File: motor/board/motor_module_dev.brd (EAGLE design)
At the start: 53.3 x 76.2 mm, 97 parts, among them IC6 LTC6088, IC7 DRV8833RTY

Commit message: Board and component orders placed
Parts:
- R2: value 5k -> 5k1
- R42: value 480R -> 470R
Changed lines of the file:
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@@
 <attribute name="VALUE" x="41.5798" y="54.2036" size="1.016" layer="27" font="vector" ratio="20" rot="R180"/>
 </element>
-<element name="R2" library="biomimetic" package="0402-RES" value="5k" x="8.255" y="33.655" smashed="yes" rot="R180">
+<element name="R2" library="biomimetic" package="0402-RES" value="5k1" x="8.255" y="33.655" smashed="yes" rot="R180">
 <attribute name="VALUE" x="7.3295" y="34.363" size="1.016" layer="27" font="vector" ratio="20" rot="R180"/>
 </element>
@@
 <attribute name="VALUE" x="18.488" y="39.6605" size="1.016" layer="27" font="vector" ratio="20" rot="R90"/>
 </element>
-<element name="C42" library="biomimetic" package="0402-CAP" value="2.2nF" x="34.29" y="36.83" smashed="yes" rot="R270"/>
+<element name="C42" library="biomimetic" package="0402-CAP" value="2.2nF" x="34.29" y="36.83" smashed="yes" rot="R270">
+<attribute name="VOLTAGE" value="6.3V" x="34.29" y="36.83" size="1.778" layer="27" rot="R270" display="off"/>
+</element>
 <element name="R31" library="biomimetic" package="0402-RES" value="1k" x="33.02" y="36.83" smashed="yes" rot="R90"/>
 <element name="C43" library="biomimetic" package="0402-CAP" value="2.2nF" x="19.05" y="34.29" smashed="yes" rot="R90">
@@
 <element name="R40" library="biomimetic" package="0402-RES" value="470R" x="45.085" y="35.56" smashed="yes" rot="R180"/>
 <element name="R41" library="biomimetic" package="0402-RES" value="470R" x="45.085" y="33.02" smashed="yes" rot="R180"/>
-<element name="R42" library="biomimetic" package="0402-RES" value="480R" x="45.085" y="30.48" smashed="yes" rot="R180">
+<element name="R42" library="biomimetic" package="0402-RES" value="470R" x="45.085" y="30.48" smashed="yes" rot="R180">
 <attribute name="VALUE" x="45.212" y="40.0245" size="1.016" layer="27" font="vector" ratio="20" rot="R270"/>
 </element>

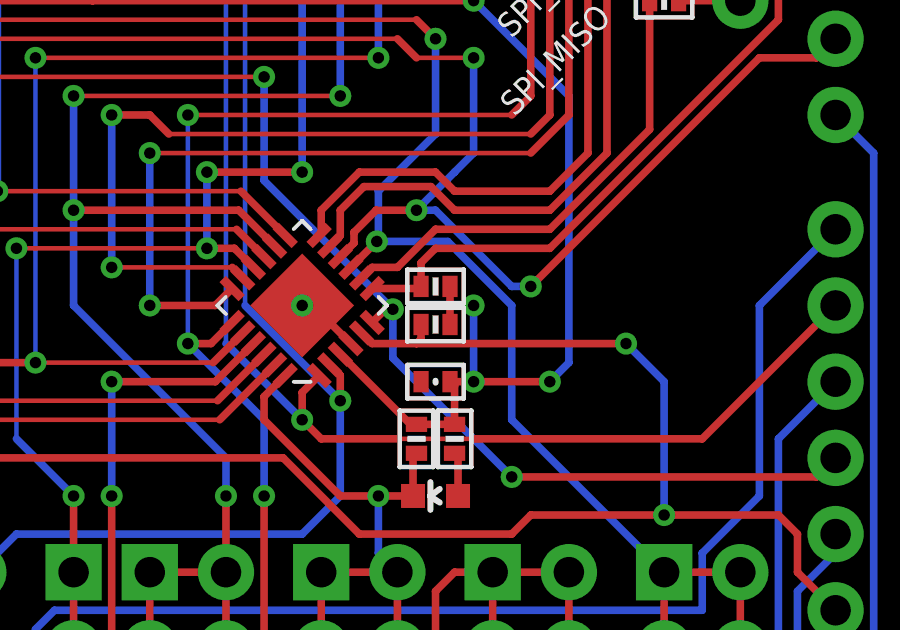
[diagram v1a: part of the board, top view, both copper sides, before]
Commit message: Moved pullup on charge management status to vbus
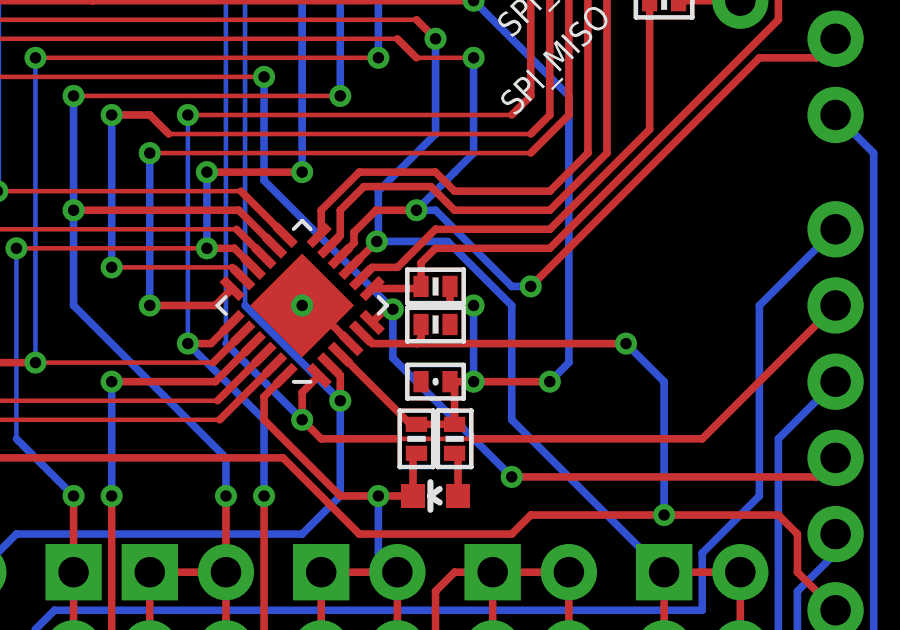
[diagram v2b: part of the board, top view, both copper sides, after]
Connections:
- net V_3.0: no longer R6.1
- net V_BUS: now also R6.1
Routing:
- net V_3.0: track 161.8 -> 161.2 mm
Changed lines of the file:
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@@
 <wire x1="5.715" y1="33.655" x2="7.62" y2="31.75" width="0.254" layer="1"/>
 <wire x1="7.62" y1="31.75" x2="7.62" y2="31.115" width="0.254" layer="1"/>
+<contactref element="R6" pad="1"/>
+<wire x1="12.065" y1="31.5976" x2="37.9476" y2="19.685" width="0" layer="19" extent="1-1"/>
 </signal>
 <signal name="N$4">
@@
 </signal>
 <signal name="V_3.0">
-<contactref element="R6" pad="1"/>
 <contactref element="C2" pad="1"/>
 <contactref element="U$11" pad="3"/>
@@
 <via x="38.735" y="20.32" extent="1-16" drill="0.381"/>
 <via x="38.735" y="17.78" extent="1-16" drill="0.381"/>
-<wire x1="37.9476" y1="20.32" x2="37.9476" y2="19.685" width="0.254" layer="1"/>
 <wire x1="38.735" y1="20.32" x2="37.9476" y2="20.32" width="0.254" layer="1"/>
 <wire x1="38.735" y1="17.78" x2="38.735" y2="20.32" width="0.254" layer="16"/>

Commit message: Working on KL05Z debugging
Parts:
- moved R6 33.6 mm to (10.9, 40.2), turned to 0 degrees
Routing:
- net CHARGE_STATUS: track 83.7 -> 87.7 mm
- net V_BUS: track 39.3 -> 41.7 mm
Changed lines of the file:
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@@
 <layer number="14" name="Route14" color="1" fill="6" visible="no" active="no"/>
 <layer number="15" name="Route15" color="4" fill="6" visible="no" active="no"/>
-<layer number="16" name="Bottom" color="1" fill="1" visible="yes" active="yes"/>
+<layer number="16" name="Bottom" color="1" fill="1" visible="no" active="yes"/>
 <layer number="17" name="Pads" color="2" fill="1" visible="yes" active="yes"/>
 <layer number="18" name="Vias" color="2" fill="1" visible="yes" active="yes"/>
 <layer number="19" name="Unrouted" color="6" fill="1" visible="yes" active="yes"/>
 <layer number="20" name="Dimension" color="15" fill="1" visible="yes" active="yes"/>
-<layer number="21" name="tPlace" color="7" fill="1" visible="no" active="yes"/>
+<layer number="21" name="tPlace" color="7" fill="1" visible="yes" active="yes"/>
 <layer number="22" name="bPlace" color="7" fill="1" visible="no" active="yes"/>
-<layer number="23" name="tOrigins" color="15" fill="1" visible="no" active="yes"/>
+<layer number="23" name="tOrigins" color="15" fill="1" visible="yes" active="yes"/>
 <layer number="24" name="bOrigins" color="15" fill="1" visible="no" active="yes"/>
 <layer number="25" name="tNames" color="7" fill="1" visible="no" active="yes"/>
 <layer number="26" name="bNames" color="7" fill="1" visible="no" active="yes"/>
-<layer number="27" name="tValues" color="7" fill="1" visible="no" active="yes"/>
+<layer number="27" name="tValues" color="7" fill="1" visible="yes" active="yes"/>
 <layer number="28" name="bValues" color="7" fill="1" visible="no" active="yes"/>
-<layer number="29" name="tStop" color="7" fill="3" visible="no" active="yes"/>
+<layer number="29" name="tStop" color="7" fill="3" visible="yes" active="yes"/>
 <layer number="30" name="bStop" color="7" fill="6" visible="no" active="yes"/>
 <layer number="31" name="tCream" color="7" fill="4" visible="no" active="yes"/>
@@
 <layer number="37" name="tTest" color="7" fill="1" visible="no" active="yes"/>
 <layer number="38" name="bTest" color="7" fill="1" visible="no" active="yes"/>
-<layer number="39" name="tKeepout" color="4" fill="11" visible="no" active="yes"/>
+<layer number="39" name="tKeepout" color="4" fill="11" visible="yes" active="yes"/>
 <layer number="40" name="bKeepout" color="1" fill="11" visible="no" active="yes"/>
 <layer number="41" name="tRestrict" color="4" fill="10" visible="no" active="yes"/>
@@
 <layer number="46" name="Milling" color="3" fill="1" visible="no" active="yes"/>
 <layer number="47" name="Measures" color="7" fill="1" visible="no" active="yes"/>
-<layer number="48" name="Document" color="7" fill="1" visible="no" active="yes"/>
+<layer number="48" name="Document" color="7" fill="1" visible="yes" active="yes"/>
 <layer number="49" name="Reference" color="7" fill="1" visible="no" active="yes"/>
 <layer number="50" name="dxf" color="7" fill="1" visible="no" active="no"/>
-<layer number="51" name="tDocu" color="7" fill="1" visible="no" active="yes"/>
+<layer number="51" name="tDocu" color="7" fill="1" visible="yes" active="yes"/>
 <layer number="52" name="bDocu" color="7" fill="1" visible="no" active="yes"/>
 <layer number="53" name="tGND_GNDA" color="7" fill="9" visible="no" active="no"/>
@@
 <attribute name="VALUE" x="12.2031" y="28.1718" size="1.016" layer="27" font="vector" ratio="20"/>
 </element>
-<element name="R6" library="biomimetic" package="0402-RES" value="10k" x="37.465" y="19.685" smashed="yes" rot="R180">
-<attribute name="VALUE" x="41.1877" y="19.8342" size="1.016" layer="27" font="vector" ratio="20" rot="R180"/>
+<element name="R6" library="biomimetic" package="0402-RES" value="10k" x="10.9" y="40.2" smashed="yes">
+<attribute name="VALUE" x="9.7773" y="38.2508" size="1.016" layer="27" font="vector" ratio="20"/>
 </element>
 <element name="R7" library="biomimetic" package="0402-RES" value="2k" x="11.43" y="41.91" smashed="yes">
-<attribute name="VALUE" x="11.0855" y="39.932" size="1.016" layer="27" font="vector" ratio="20"/>
+<attribute name="VALUE" x="9.8855" y="42.732" size="1.016" layer="27" font="vector" ratio="20"/>
 </element>
 <element name="C1" library="biomimetic" package="0402-CAP" value="2.2uF" x="12.065" y="31.115" smashed="yes" rot="R270">
@@
 <attribute name="DESIGN" value="Motor Control Dev" x="1.27" y="71.12" size="1.016" layer="21" font="vector" ratio="20"/>
 <attribute name="ORGANIZATION" value="UC Berkeley Biomimetic Millisystems Lab" x="1.27" y="72.39" size="1.016" layer="21" font="vector" ratio="20"/>
-<attribute name="REVISION" value="r0.0" x="16.51" y="71.12" size="1.016" layer="21" font="vector" ratio="20"/>
+<attribute name="REVISION" value="r0.1" x="16.51" y="71.12" size="1.016" layer="21" font="vector" ratio="20"/>
 </element>
 </elements>
@@
 <wire x1="7.62" y1="31.75" x2="7.62" y2="31.115" width="0.254" layer="1"/>
 <contactref element="R6" pad="1"/>
-<wire x1="12.065" y1="31.5976" x2="37.9476" y2="19.685" width="0" layer="19" extent="1-1"/>
+<wire x1="8.89" y1="41.91" x2="10.4174" y2="40.3826" width="0.254" layer="1"/>
+<wire x1="10.4174" y1="40.3826" x2="10.4174" y2="40.2" width="0.254" layer="1"/>
 </signal>
 <signal name="N$4">
@@
 <contactref element="U$27" pad="D2"/>
 <wire x1="34.999896875" y1="19.400759375" x2="35.35065625" y2="19.05" width="0.254" layer="1"/>
-<wire x1="43.815" y1="19.05" x2="36.83" y2="19.05" width="0.254" layer="1"/>
-<wire x1="36.83" y1="19.05" x2="35.35065625" y2="19.05" width="0.254" layer="1"/>
+<wire x1="43.815" y1="19.05" x2="35.35065625" y2="19.05" width="0.254" layer="1"/>
 <wire x1="32.385" y1="15.24" x2="19.05" y2="15.24" width="0.254" layer="1"/>
 <via x="43.815" y="19.05" extent="1-16" drill="0.381"/>
@@
 <wire x1="40.005" y1="12.7" x2="40.64" y2="13.335" width="0.254" layer="1"/>
 <wire x1="40.64" y1="13.335" x2="45.085" y2="13.335" width="0.254" layer="1"/>
-<wire x1="36.9824" y1="19.685" x2="36.9824" y2="19.2024" width="0.254" layer="1"/>
-<wire x1="36.9824" y1="19.2024" x2="36.83" y2="19.05" width="0.254" layer="1"/>
 <via x="19.05" y="15.24" extent="1-16" drill="0.381"/>
 <via x="13.97" y="43.18" extent="1-16" drill="0.381"/>
@@
 <wire x1="20.32" y1="16.51" x2="20.32" y2="17.78" width="0.254" layer="16"/>
 <wire x1="20.32" y1="17.78" x2="13.97" y2="24.13" width="0.254" layer="16"/>
+<wire x1="11.3826" y1="40.2" x2="11.4826" y2="40.3" width="0.254" layer="1"/>
+<wire x1="11.4826" y1="40.3" x2="12.6" y2="40.3" width="0.254" layer="1"/>
+<wire x1="12.6" y1="40.3" x2="13.97" y2="41.67" width="0.254" layer="1"/>
+<wire x1="13.97" y1="41.67" x2="13.97" y2="43.18" width="0.254" layer="1"/>
 </signal>
 <signal name="V_3.0">
@@
 <wire x1="40.005" y1="14.605" x2="36.0426" y2="18.5674" width="0.254" layer="16"/>
 <wire x1="36.0426" y1="18.5674" x2="36.0426" y2="20.193" width="0.254" layer="16"/>
-<wire x1="10.9474" y1="41.91" x2="10.9474" y2="37.3126" width="0.254" layer="1"/>
 <wire x1="10.9474" y1="37.3126" x2="20.32" y2="27.94" width="0.254" layer="1"/>
 <wire x1="20.32" y1="27.94" x2="31.75" y2="27.94" width="0.1524" layer="1"/>
@@
 <wire x1="31.75" y1="27.94" x2="31.75" y2="24.4856" width="0.254" layer="16"/>
 <wire x1="31.75" y1="24.4856" x2="36.0426" y2="20.193" width="0.254" layer="16"/>
+<wire x1="10.9474" y1="41.91" x2="10.9" y2="41.91" width="0.1524" layer="1"/>
+<wire x1="10.9" y1="41.91" x2="10.9" y2="37.3126" width="0.1524" layer="1"/>
+<wire x1="10.9" y1="37.3126" x2="10.9474" y2="37.3126" width="0.1524" layer="1"/>
 </signal>
 <signal name="N$6">
